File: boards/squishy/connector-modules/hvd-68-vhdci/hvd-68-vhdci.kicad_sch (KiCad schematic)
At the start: 14 parts, among them J1 SCSI PHY Mezz, J2 Conn_02x25_Odd_Even, J3 Conn_01x04, J4 Conn_02x34_Clockwise_Shield, J5 Conn_02x24_Clockwise_Shield, U1 M24C02-RMC

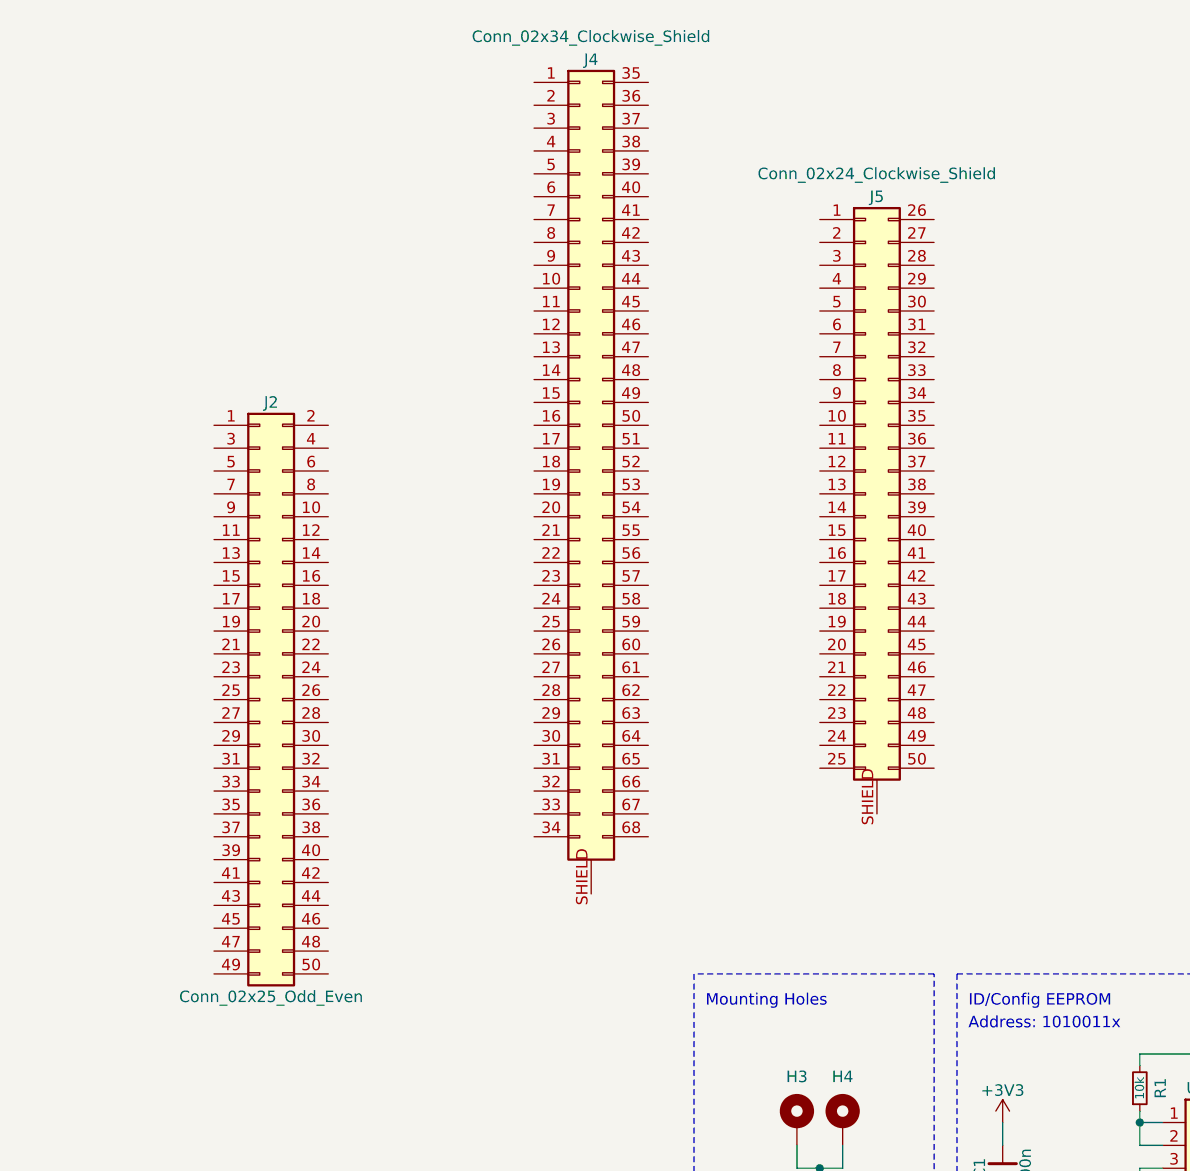
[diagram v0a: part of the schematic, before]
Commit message: squishy: connectors: Removed unneeded connector symbols in the given kicad schematics
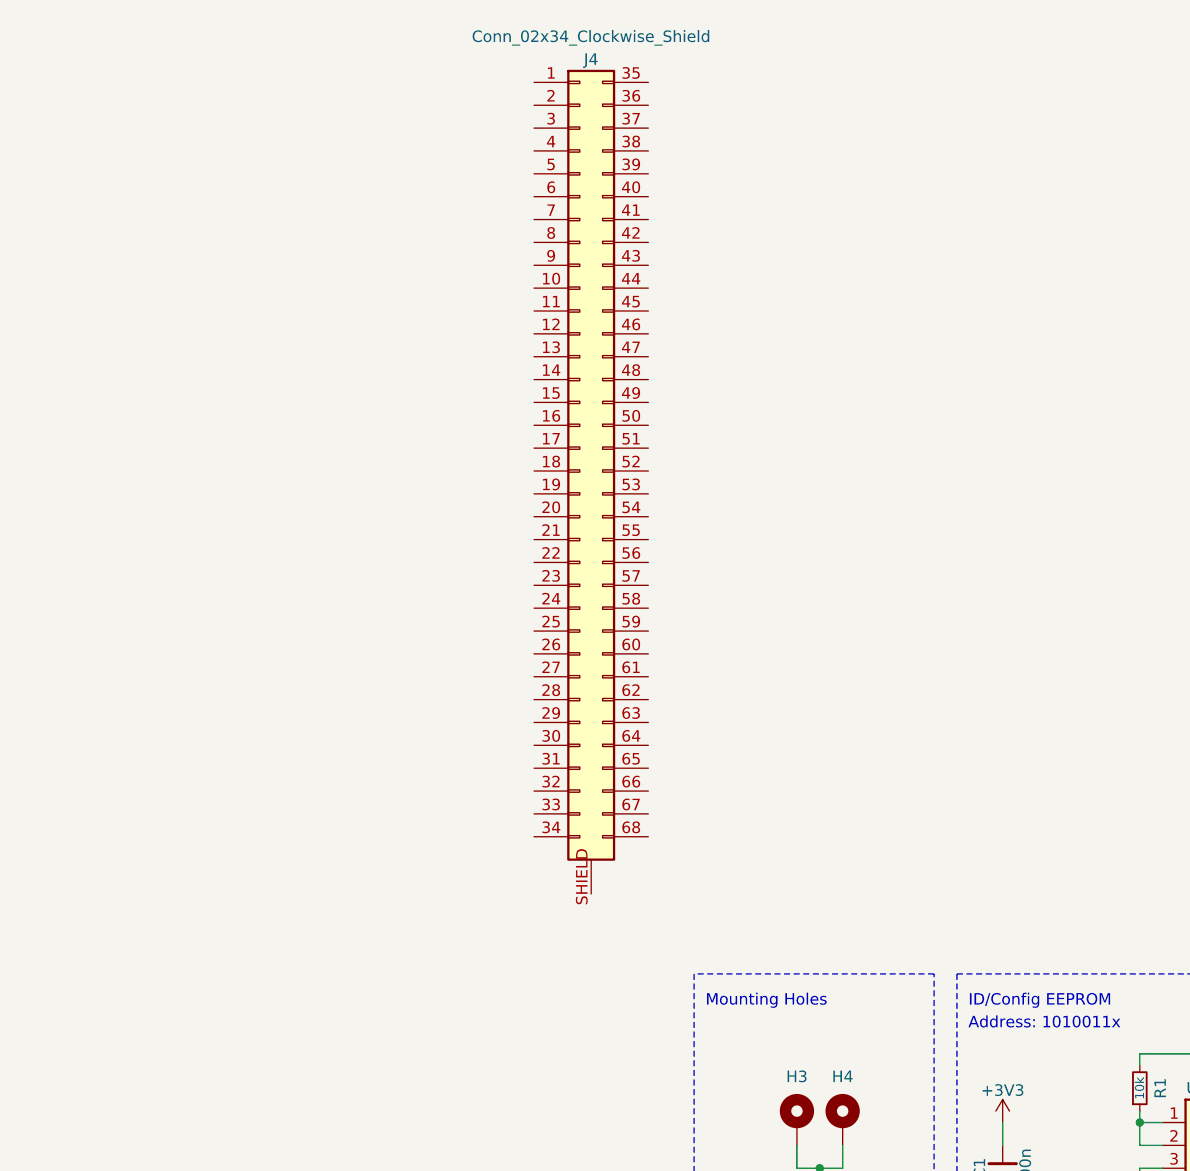
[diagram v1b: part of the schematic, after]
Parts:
- removed J2: Conn_02x25_Odd_Even, Connector_IDC:IDC-Header_2x25_P2.54mm_Horizontal, symbol Connector_Generic:Conn_02x25_Odd_Even
- removed J5: Conn_02x24_Clockwise_Shield, symbol lethalbit-connectors:Conn_02x25_Counter_Clockwise

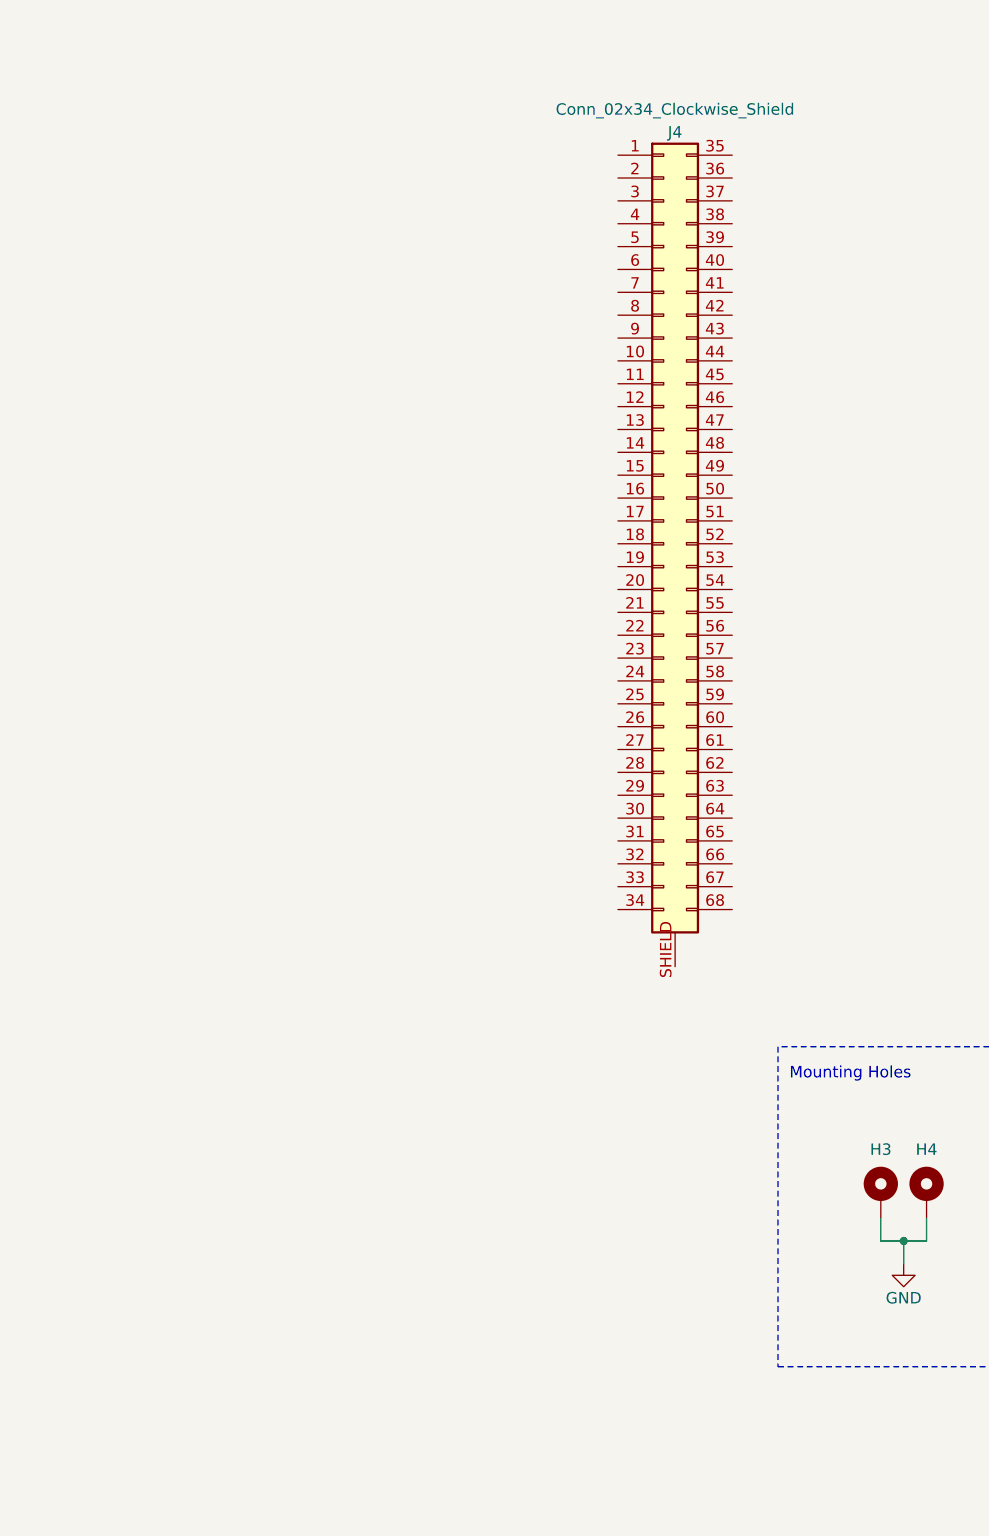
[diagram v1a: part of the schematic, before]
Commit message: squishy: connectors: hooked up hd-68-vhdci connector
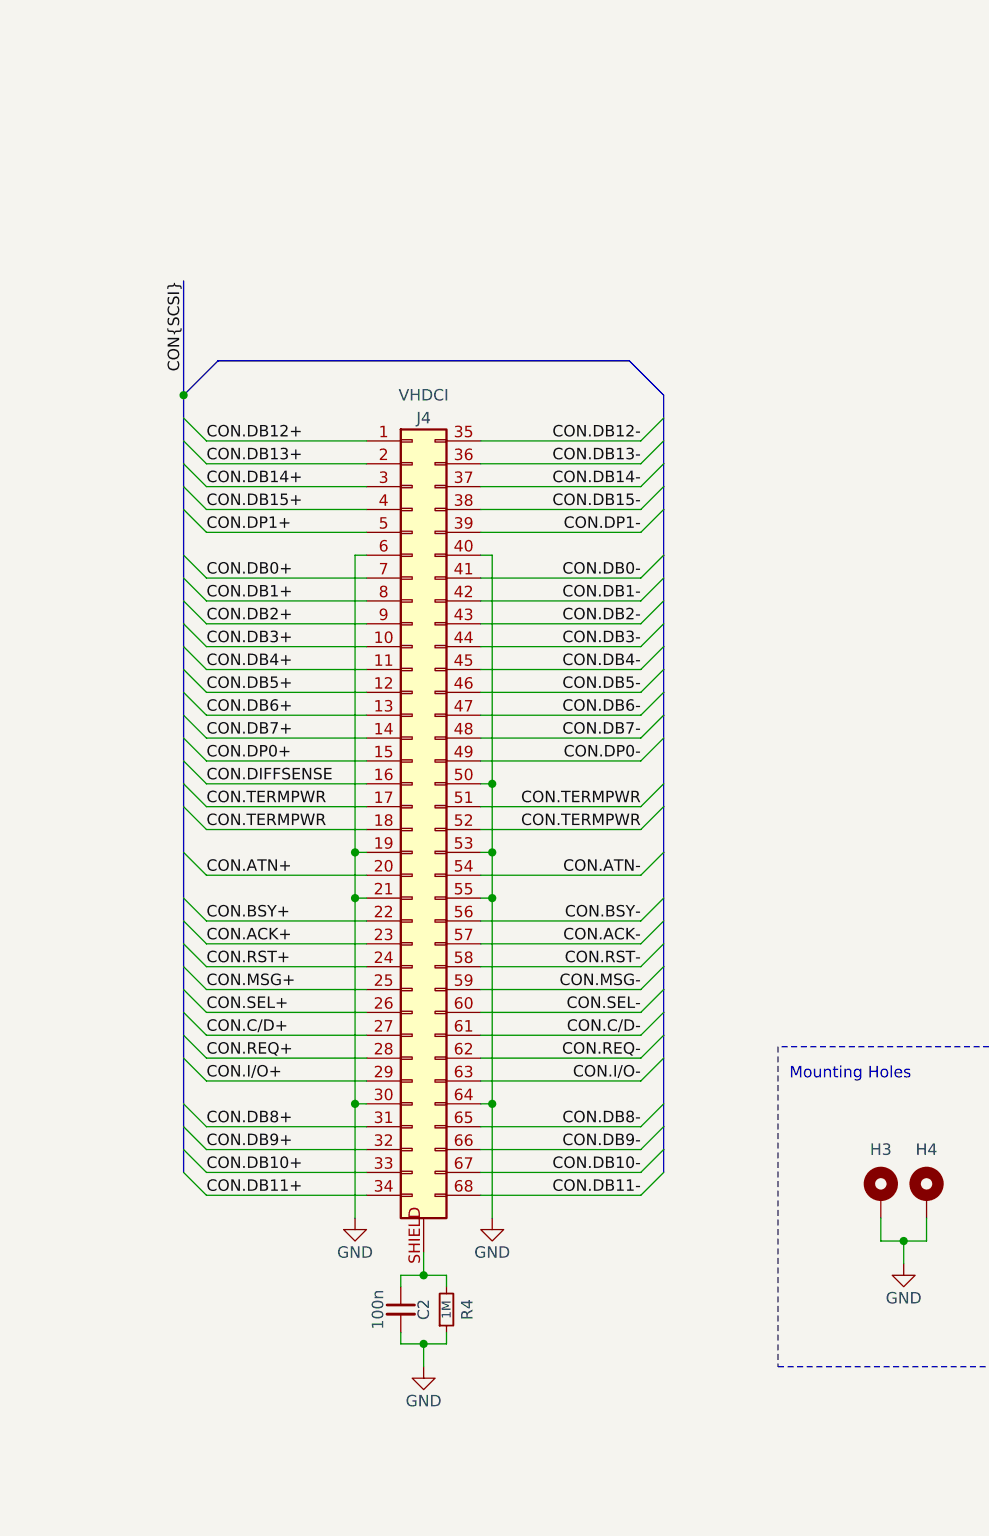
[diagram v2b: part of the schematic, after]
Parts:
- added C2: 100n, rhais_rcl:C0603, symbol Device:C_Small
- added R4: 1M, rhais_rcl:R0603, symbol Device:R_Small
- J4: value Conn_02x34_Clockwise_Shield -> VHDCI; footprint (none) -> lethalbit-connectors:5796055
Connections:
- net CON.ACK+: now also J4.23 (Pin_23)
- net CON.ACK-: now also J4.57 (Pin_57)
- net CON.ATN+: now also J4.20 (Pin_20)
- net CON.ATN-: now also J4.54 (Pin_54)
- net CON.BSY+: now also J4.22 (Pin_22)
- net CON.BSY-: now also J4.56 (Pin_56)
- net CON.C/D+: now also J4.27 (Pin_27)
- net CON.C/D-: now also J4.61 (Pin_61)
- net CON.DB0+: now also J4.7 (Pin_7)
- net CON.DB0-: now also J4.41 (Pin_41)
- net CON.DB1+: now also J4.8 (Pin_8)
- net CON.DB1-: now also J4.42 (Pin_42)
- net CON.DB10+: now also J4.33 (Pin_33)
- net CON.DB10-: now also J4.67 (Pin_67)
- net CON.DB11+: now also J4.34 (Pin_34)
- net CON.DB11-: now also J4.68 (Pin_68)
- net CON.DB13+: now also J4.2 (Pin_2)
- net CON.DB13-: now also J4.36 (Pin_36)
- net CON.DB15+: now also J4.4 (Pin_4)
- net CON.DB15-: now also J4.38 (Pin_38)
- net CON.DB2+: now also J4.9 (Pin_9)
- net CON.DB2-: now also J4.43 (Pin_43)
- net CON.DB3+: now also J4.10 (Pin_10)
- net CON.DB3-: now also J4.44 (Pin_44)
- net CON.DB4+: now also J4.11 (Pin_11)
- net CON.DB4-: now also J4.45 (Pin_45)
- net CON.DB5+: now also J4.12 (Pin_12)
- net CON.DB5-: now also J4.46 (Pin_46)
- net CON.DB6+: now also J4.13 (Pin_13)
- net CON.DB6-: now also J4.47 (Pin_47)
- net CON.DB7+: now also J4.14 (Pin_14)
- net CON.DB7-: now also J4.48 (Pin_48)
- net CON.DB8+: now also J4.31 (Pin_31)
- net CON.DB8-: now also J4.65 (Pin_65)
- net CON.DB9+: now also J4.32 (Pin_32)
- net CON.DB9-: now also J4.66 (Pin_66)
- net CON.DIFFSENSE: now also J4.16 (Pin_16)
- net CON.DP0+: now also J4.15 (Pin_15)
- net CON.DP0-: now also J4.49 (Pin_49)
- net CON.DP1+: now also J4.5 (Pin_5)
- net CON.DP1-: now also J4.39 (Pin_39)
- net CON.I/O+: now also J4.29 (Pin_29)
- net CON.I/O-: now also J4.63 (Pin_63)
- net CON.MSG+: now also J4.25 (Pin_25)
- net CON.MSG-: now also J4.59 (Pin_59)
- net CON.REQ+: now also J4.28 (Pin_28)
- net CON.REQ-: now also J4.62 (Pin_62)
- net CON.RST+: now also J4.24 (Pin_24)
- net CON.RST-: now also J4.58 (Pin_58)
- net CON.SEL+: now also J4.26 (Pin_26)
- net CON.SEL-: now also J4.60 (Pin_60)
- net CON.TERMPWR: now also J4.17 (Pin_17), J4.18 (Pin_18), J4.51 (Pin_51), J4.52 (Pin_52)
- net GND: now also J4.19 (Pin_19), J4.21 (Pin_21), J4.30 (Pin_30), J4.40 (Pin_40), J4.50 (Pin_50), J4.53 (Pin_53), J4.55 (Pin_55), J4.6 (Pin_6), J4.64 (Pin_64), C2.2, R4.1
- net CON.DB12+: now reaches J4.1 (Pin_1)
- net CON.DB14+: now reaches J4.3 (Pin_3)
- net CON.DB12-: now reaches J4.35 (Pin_35)
- net CON.DB14-: now reaches J4.37 (Pin_37)
- net at J4.SHIELD: now also C2.1, R4.2
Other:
- moved on the sheet: J4

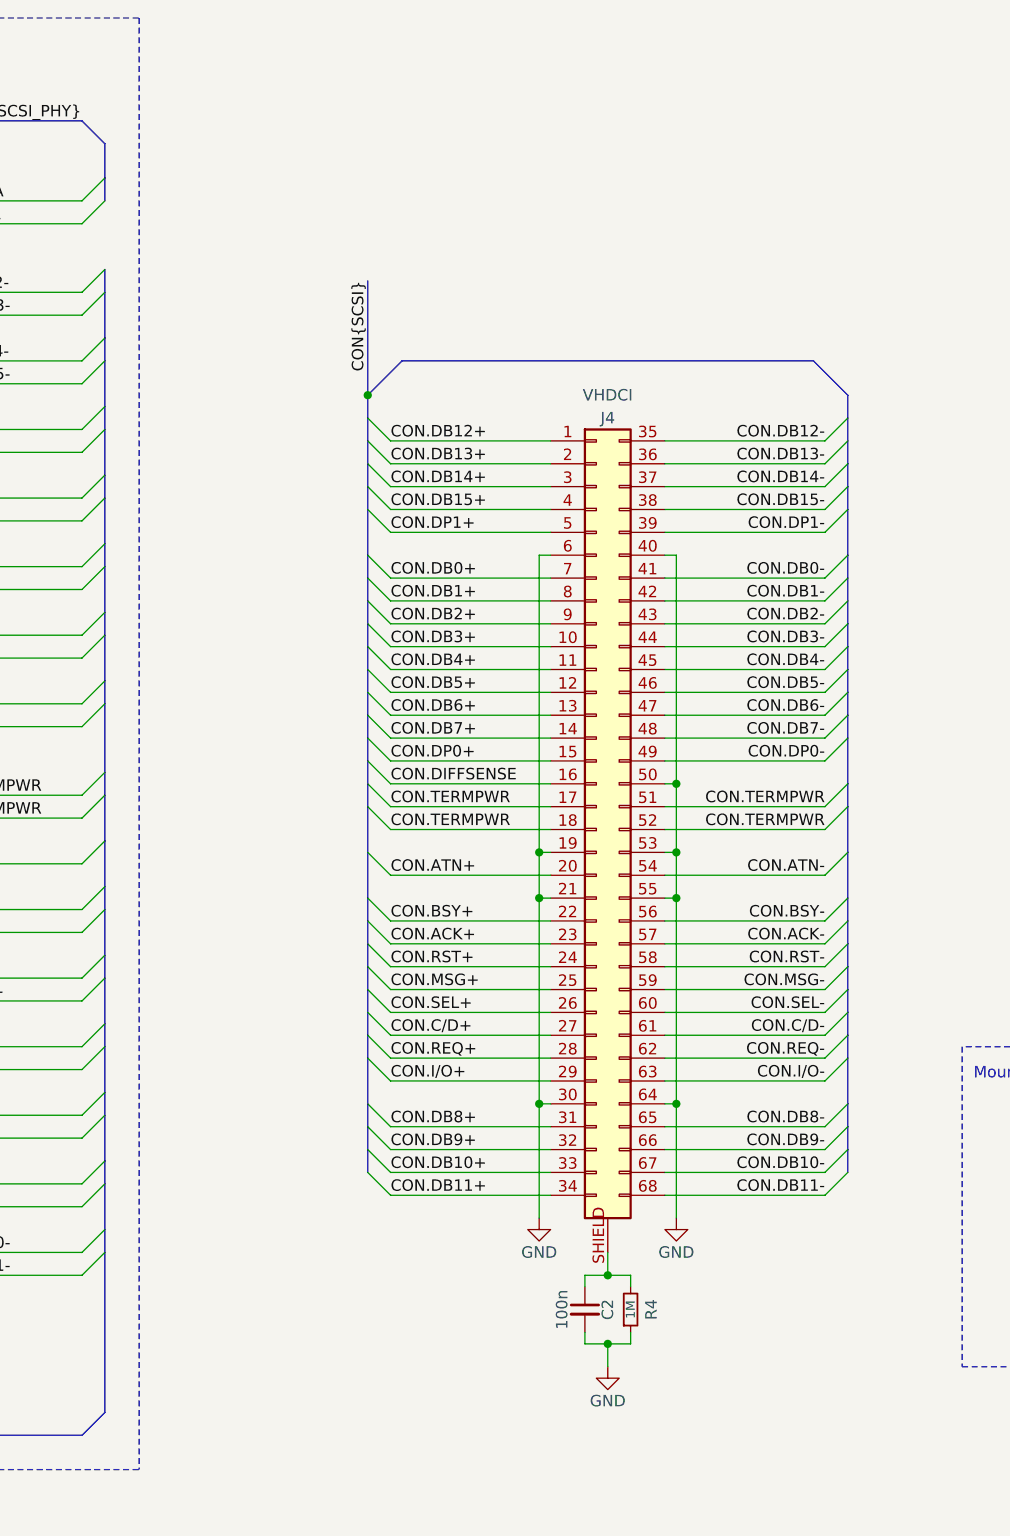
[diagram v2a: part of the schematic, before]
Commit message: squishy: connectors: Cleaned up and unified look/feel of connector schematics
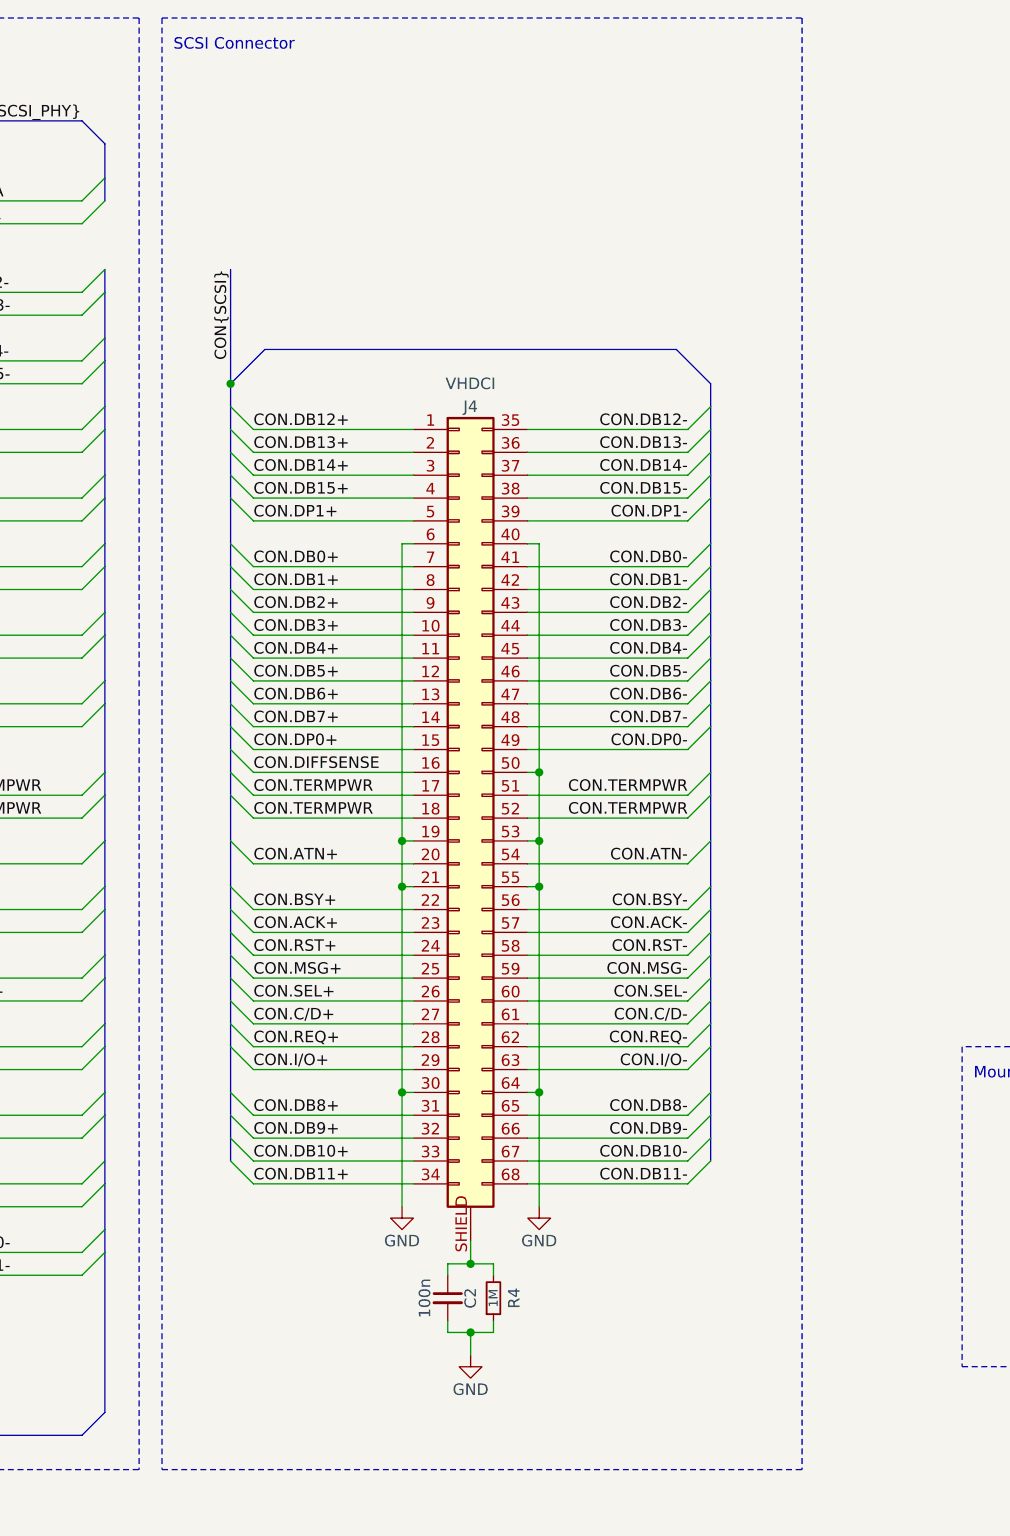
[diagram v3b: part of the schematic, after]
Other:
- note added: "SCSI Connector"
- moved on the sheet: C2, J4, R4

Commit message: squishy: connectors: updated schematic title blocks for connectors as appropriate
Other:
- title: Squishy -  ICD 50 -> Squishy -  SCSI HVD VHDCI Connector Module
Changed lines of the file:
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@@
 	(paper "A4")
 	(title_block
-		(title "Squishy -  ICD 50")
-		(date "2024-08-22")
+		(title "Squishy -  SCSI HVD VHDCI Connector Module")
+		(date "2024-09-17")
 		(rev "1")
 		(company "Shrine Maiden Heavy Industries")
